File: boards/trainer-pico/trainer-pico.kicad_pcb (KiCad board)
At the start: 2 copper layers, 132.1 x 99.1 mm, 36 parts, among them J1 Conn_01x08_Pin, J10 Conn_01x04_Socket, J11 Conn_01x17_Pin, J12 Conn_01x17_Socket, J13 Conn_01x17_Socket, J14 Conn_01x17_Pin, J15 Barrel_Jack_Switch, J16 Conn_01x04_Pin, J17 Conn_01x04_Pin, J18 Conn_01x04_Pin, J2 Conn_01x04_Pin, J3 Conn_01x06_Pin, J4 Conn_01x04_Pin, J5 Conn_01x04_Pin, J6 Conn_01x08_Socket, J7 Conn_01x04_Socket, J8 Conn_01x06_Socket, J9 Conn_01x04_Socket, U2 L7805, U3 L7809

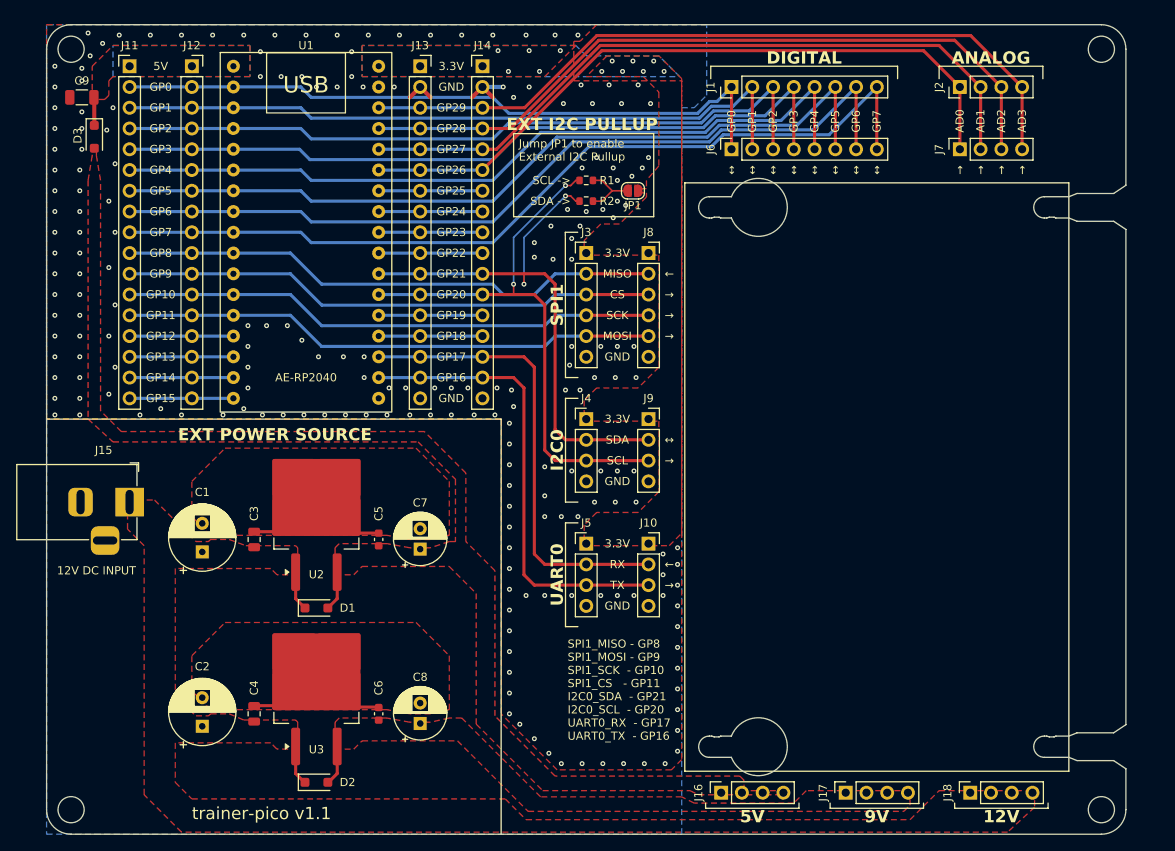
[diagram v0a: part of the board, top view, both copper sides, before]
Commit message: 不要部分を除去
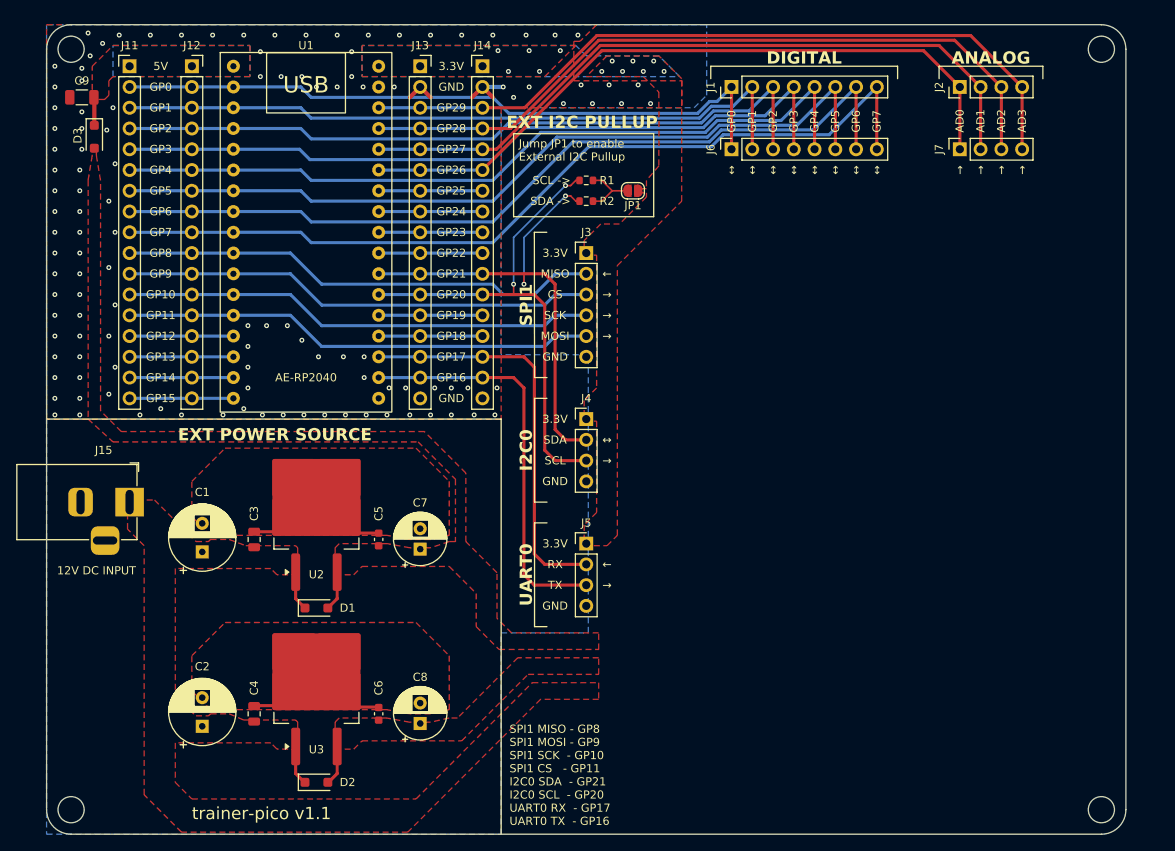
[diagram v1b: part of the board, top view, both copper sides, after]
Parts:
- removed J10, J9: Conn_01x04_Socket, Connector_PinSocket_2.54mm:PinSocket_1x04_P2.54mm_Vertical
- removed J16, J17, J18: Conn_01x04_Pin, Connector_PinSocket_2.54mm:PinSocket_1x04_P2.54mm_Vertical
- removed J8: Conn_01x06_Socket, Connector_PinSocket_2.54mm:PinSocket_1x06_P2.54mm_Vertical
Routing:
- net /SPI_MOSI: track 65.6 -> 58.0 mm
- net /UART_PICO_TX: track 56.9 -> 49.3 mm
- net /UART_PICO_RX: track 56.9 -> 49.3 mm
- net /SPI_SCK: track 65.6 -> 58.0 mm
- net /SPI_MISO: track 66.7 -> 59.0 mm
- net /SPI_CS: track 65.6 -> 58.0 mm
- net /I2C_SDA: track 68.0 -> 60.4 mm
- net /I2C_SCL: track 69.8 -> 62.2 mm
- net GND: vias 207 -> 119
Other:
- outline, holes or cut-outs redrawn
- board text added: "SPI1 MISO - GP8 SPI1 MOSI - GP9 SPI1 SCK - GP10 SPI1 CS - GP11 I2C0 SDA - GP21 I2C0 SCL - GP20 UART0 RX - GP17 UART0 TX - GP16"
- board text removed: "12V"
- board text removed: "9V"
- board text removed: "SPI1_MISO - GP8 SPI1_MOSI - GP9 SPI1_SCK - GP10 SPI1_CS - GP11 I2C0_SDA - GP21 I2C0_SCL - GP20 UART0_RX - GP17 UART0_TX - GP16"

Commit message: 電源のテストポイントを追加
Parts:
- added TP1: TestPoint, Connector_PinHeader_2.54mm:PinHeader_1x01_P2.54mm_Vertical, F.Cu at (53.3, 124.5)
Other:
- board text added: "12V"
- board text added: "9V"
